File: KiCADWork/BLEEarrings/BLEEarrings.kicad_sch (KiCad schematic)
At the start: 16 parts, among them Q1 DMP3013SFV, SW1 PB22E06071, U1 XB6096I2SV, U2 MCP73831T-2ACI/OT, U3 GT-USB-7010ASV, U4 2.0MM-2P WZ MS

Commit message: More KiCAD Work
More KiCAD work complete
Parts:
- removed C1, C3: 10u, Capacitor_SMD:C_0402_1005Metric_Pad0.74x0.62mm_HandSolder, symbol Device:C
- removed C2: 100n, Capacitor_SMD:C_0402_1005Metric_Pad0.74x0.62mm_HandSolder, symbol Device:C
- removed Q1: DMP3013SFV, Package_SON:Diodes_PowerDI3333-8, symbol Transistor_FET:DMP3013SFV
- removed R3: 2k, Resistor_SMD:R_0402_1005Metric, symbol Device:R
- removed R4: 3k3, Resistor_SMD:R_0402_1005Metric, symbol Device:R
- removed R5: 100, Resistor_SMD:R_0402_1005Metric, symbol Device:R
- removed R6, R7: 5k1, Resistor_SMD:R_0402_1005Metric, symbol Device:R
- removed SW1: PB22E06071, easyeda2kicad:SW-TH_6P-L5.8-W5.8-P2.00-LS4.5_PB22E06371-0625, symbol easyeda2kicad:PB22E06071
- removed U1: XB6096I2SV, easyeda2kicad:WDFN-6_L2.0-W2.0-P0.65-BL-EP, symbol easyeda2kicad:XB6096I2SV
- removed U2: MCP73831T-2ACI/OT, easyeda2kicad:SOT-23-5_L3.0-W1.7-P0.95-LS2.8-BL, symbol easyeda2kicad:MCP73831T-2ACI_OT
- R1: value 2k -> 5k1
- R2: value 4k99 -> 5k1
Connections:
- net GND: now also R1.2
- net Power/VBAT: now reaches U4.1
- net Power/BATGND: now reaches U4.2
- net at U3.A5 (CC1): now also R2.1
- net at U3.B5 (CC2): now also R1.1
- net VBus renamed Power/VBUS
- net Power/VBUS: no longer R1.1
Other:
- added sheet DSP (DSP.kicad_sch)
- added sheet Power (Power.kicad_sch)
- moved on the sheet: U3, U4

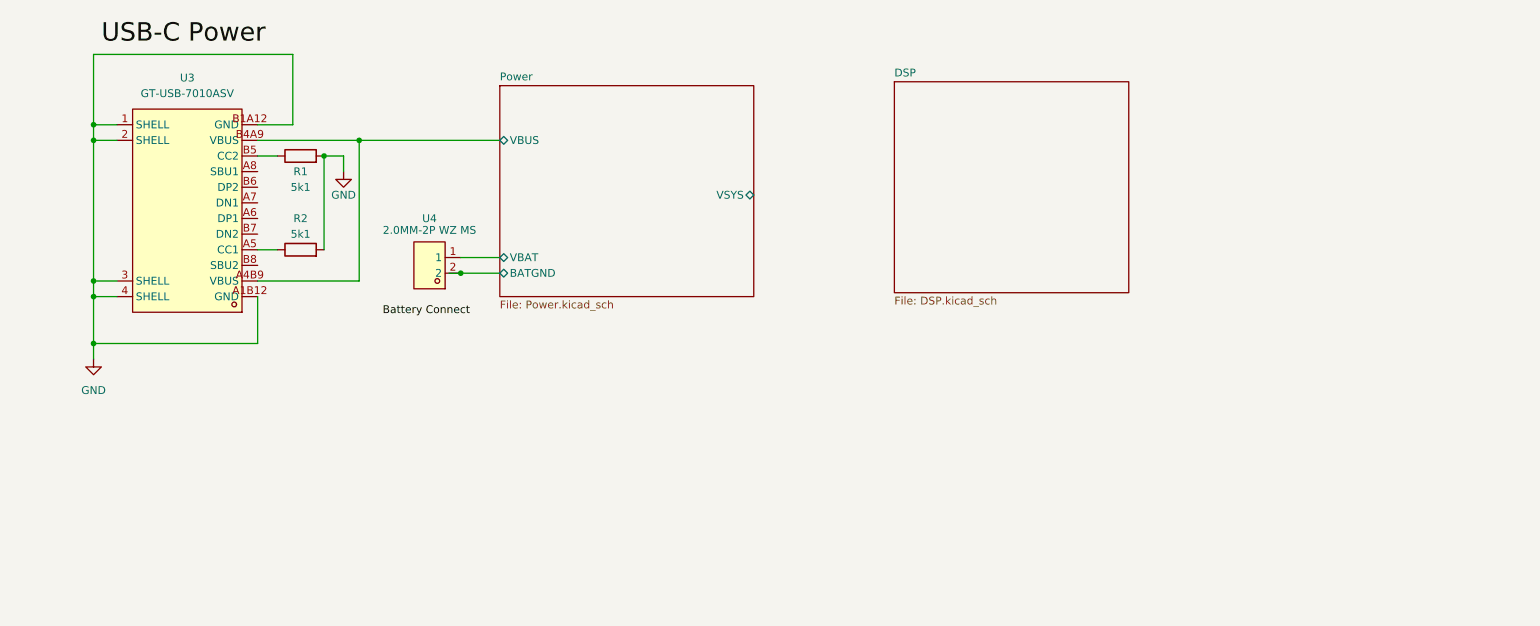
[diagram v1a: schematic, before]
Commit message: First Draft Schematic Done
- Symbols and footprints checked
- Dom added to repo
- Centralised footprints created
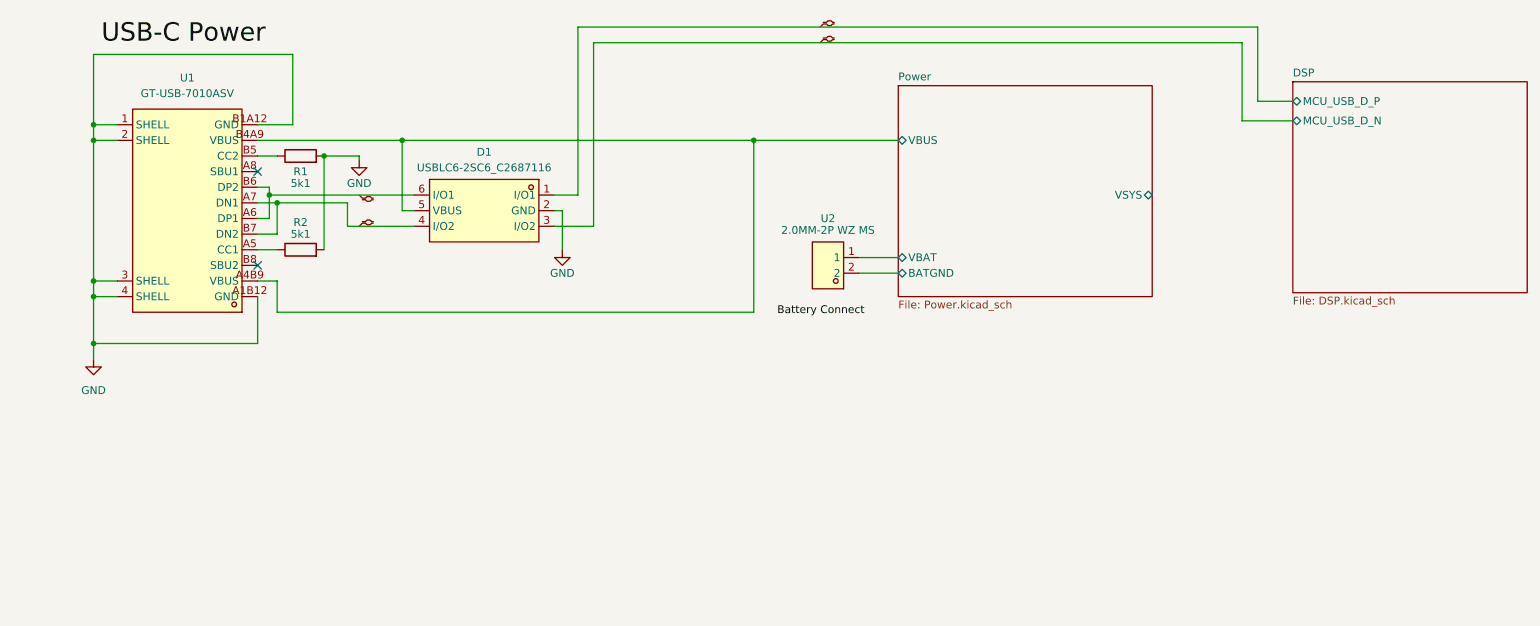
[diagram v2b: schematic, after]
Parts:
- added D1: USBLC6-2SC6_C2687116, easyeda2kicad:SOT-23-6_L2.9-W1.6-P0.95-LS2.8-BL, symbol easyeda2kicad:USBLC6-2SC6_C2687116
- added MP1, MP2, MP3, MP4: ~, symbol CustomPads:Matched_Impedance
- R1, R2: footprint Resistor_SMD:R_0402_1005Metric -> Resistor_SMD:R_0402_1005Metric_Pad0.72x0.64mm_HandSolder
- U1: renamed from U3; footprint easyeda2kicad:USB-C-SMD_G-SWITCH_GT-USB-7010ASV -> easyeda2kicad:USB-C-TH_12401832E402A
- renumbered U4 to U2
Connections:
- net GND: now also D1.2 (GND)
- net Power/VBUS: now also D1.5 (VBUS)
- net at U1.A6 (DP1): now also U1.B6 (DP2), D1.6 (I/O1)
- net at U1.A7 (DN1): now also U1.B7 (DN2), D1.4 (I/O2)
- new net DSP/MCU_USB_D_N: D1.3 (I/O2)
- new net DSP/MCU_USB_D_P: D1.1 (I/O1)
- no-connect marks 0 -> 2
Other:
- sheet DSP ports: added MCU_USB_D_N, MCU_USB_D_P; removed none
- company: (none) -> Kitty and Dom
- title: (none) -> BLEEarrings (Blade Runner)
- moved on the sheet: U2

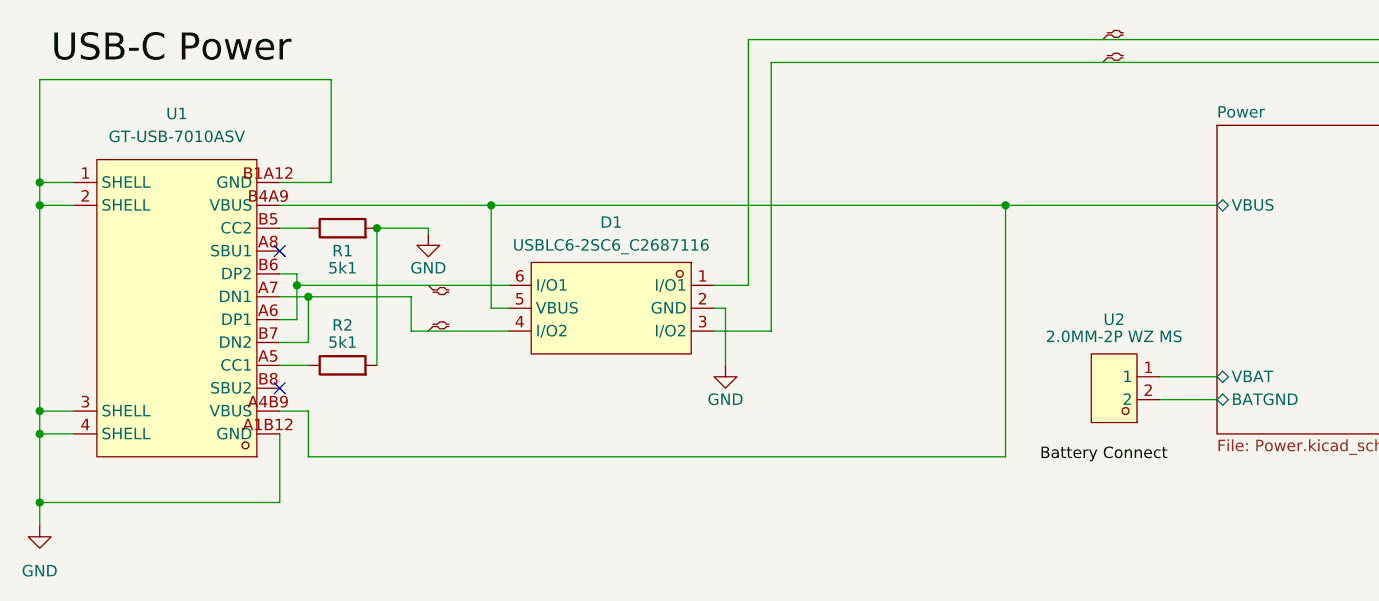
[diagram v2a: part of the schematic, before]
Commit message: Improved Antenna Layout
- Initial layout complete
- TO DO:
    - Test points
    - Curved Tracks
    - Silkscreen
    - Check antenna
    - create casing in blender
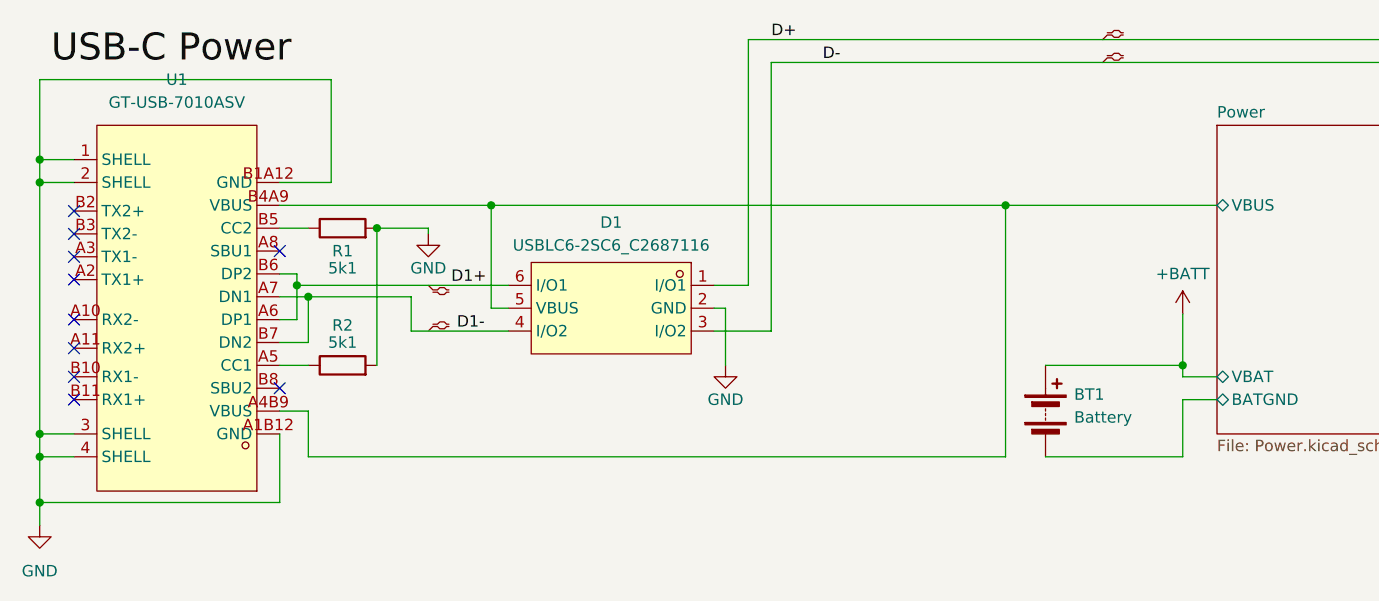
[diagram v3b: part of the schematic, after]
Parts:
- removed U2: 2.0MM-2P WZ MS, easyeda2kicad:CONN-TH_2P-P2.00_SHOUHAN_2.0MM-2P-WZ-MS, symbol easyeda2kicad:2.0MM-2PWZMS
- added BT1: Battery, easyeda2kicad:BAT-TH_BS-24-A1AJ013, symbol Device:Battery
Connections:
- net Power/BATGND: now also BT1.2 (-)
- net D1-: now reaches D1.4 (I/O2), U1.A7 (DN1), U1.B7 (DN2)
- net D1+: now reaches D1.6 (I/O1), U1.A6 (DP1), U1.B6 (DP2)
- net DSP/MCU_USB_D_N renamed D-
- net DSP/MCU_USB_D_P renamed D+
- new net +BATT: BT1.1 (+)
- no-connect marks 2 -> 10
